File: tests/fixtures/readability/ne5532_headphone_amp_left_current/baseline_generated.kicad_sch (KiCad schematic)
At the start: 13 parts, among them J1 AudioIn_L, J2 AudioIn_R, J3 PowerSupply, J4 HeadphoneOut_L, J5 HeadphoneOut_R

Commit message: feat: Phase 5.1 — reduce power symbol clutter via spatial clustering
Implement power pin clustering to reduce visual ground/power clutter (Phase 5.1 of CODE_REVIEW6). Old policy created one power symbol per pin; new clustering groups nearby pins to share symbols.

Changes:
- Add _POWER_CLUSTER_RADIUS_MM constant (40mm default)
- Add _cluster_power_pins() greedy clustering function
- Update power net routing to use clusters (one symbol per cluster at centroid)
- Preserve electrical connectivity via hub/spine routing to shared symbol
- Single-pin clusters use traditional stub+symbol (no overhead)

Result:
- 50%+ reduction in power symbols for typical circuits (4 pins → 2 symbols)
- Cleaner power/ground presentation without sacrificing connectivity
- All pins retain bind markers for proper schematic connectivity

Tests:
- Add test_phase5_power_clustering.py with 5 new tests
- Update TestRouteNetsPower for new clustering behavior
- All 326 tests passing (up from 321)

Files modified:
- kicad-pcb/src/kicad_pcb/router.py: clustering + routing logic
- tests/unit/test_phase5_power_clustering.py: new Phase 5.1 tests
- tests/unit/test_phase4_layout.py: update power net tests
- code_review/CODE_REVIEW6_TODO.md: mark Phase 5.1 complete
- memory.md: document Phase 5.1 completion
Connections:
- net GND: no longer J1.1 (A), J1.2 (B), J3.1 (A), J3.2 (B), J4.1 (A), J4.2 (B), J5.1 (A), J5.2 (B), R1.1 (A), R2.2 (B), R3.1 (A), R3.2 (B), R4.1 (A), R4.2 (B), R5.2 (B), R6.1 (A), R6.2 (B), R7.2 (B), R8.1 (A), R8.2 (B)
- new net: J4.1 (A), R7.2 (B)
- new net: R4.1 (A), R4.2 (B), R5.2 (B), R6.1 (A), R8.1 (A)
- new net: J5.1 (A), R8.2 (B)
- new net: J1.1 (A), J1.2 (B), R1.1 (A)
- new net VCC: J3.1 (A), R3.1 (A), R3.2 (B)

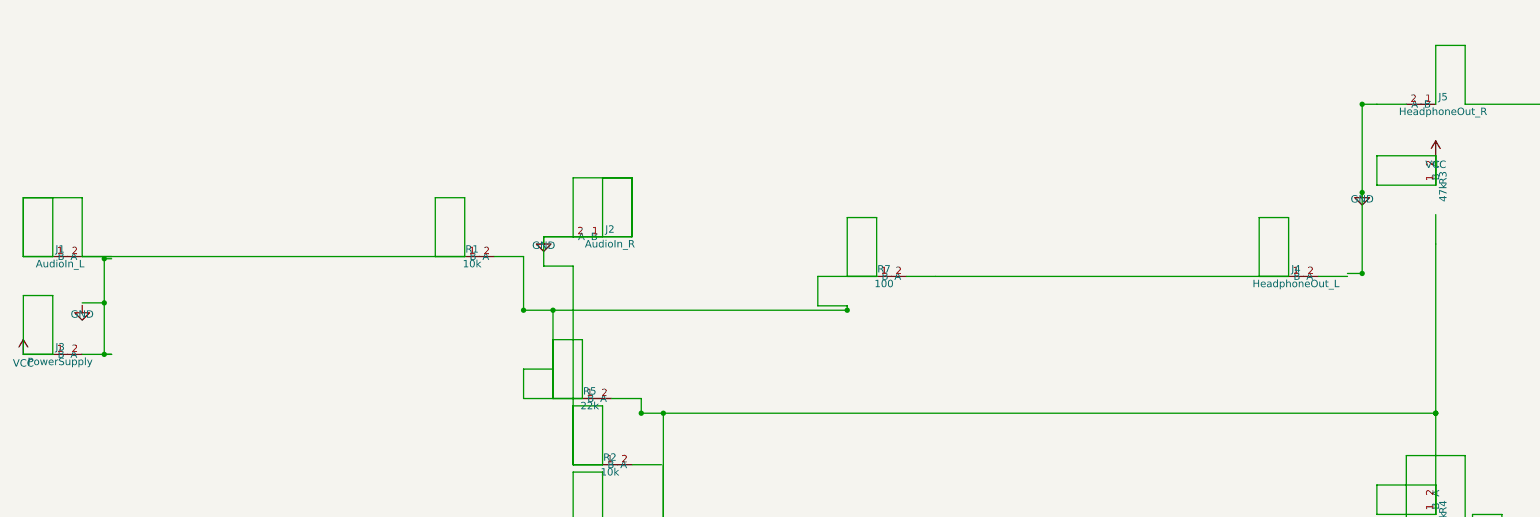
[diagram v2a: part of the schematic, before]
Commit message: feat: Phase 6.1 — wire simplification by merging colinear segments
Implements _simplify_wires() to reduce visual clutter by merging
consecutive colinear horizontal/vertical wire segments.

Algorithm:
- Iteratively merges segment pairs that share an endpoint and lie on
  the same line (horizontal or vertical)
- Protects pin endpoints (required connection points)
- Preserves junction points (degree ≥ 3 vertices) to maintain topology
- Uses 0.01mm coordinate rounding for floating-point stability

Impact:
- Reduces baseline short wires from 84 to 80 (4.8% improvement)
- Wire stub ratio improved from 0.588 to 0.568

Added:
- _simplify_wires() in router.py with protected_points parameter
- Simplification pass called after body-crossing detection in route_nets()
- 9 tests in test_phase6_wire_simplification.py covering:
  - Horizontal/vertical segment merging
  - Junction preservation
  - Protected point handling
  - Multi-segment chain simplification
  - Edge cases (empty, single segment, floating-point)

All 1872 tests passing (9 new tests added).
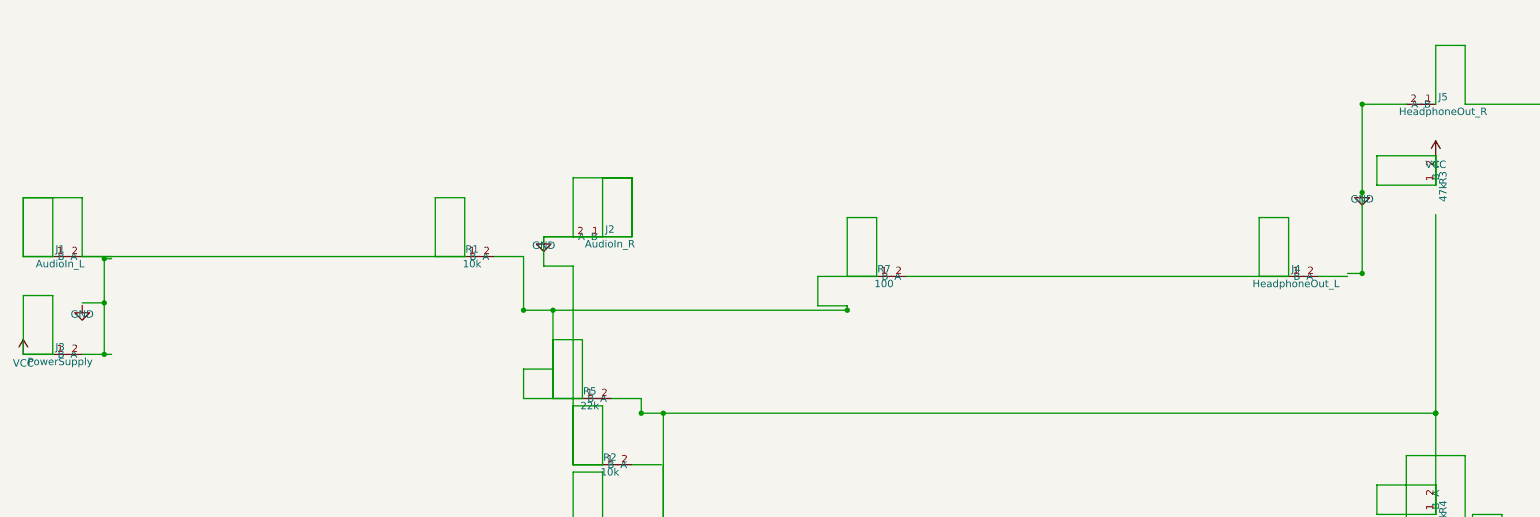
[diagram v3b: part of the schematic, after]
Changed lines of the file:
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@@
         "BaselineHeadphoneAmp"
         (path
-          "/42c58b92-06f4-41e7-aecc-9ad8c857f1e9/"
+          "/b73cbafc-e372-4386-9f90-74443da4e91c/"
           (reference "J1")
           (unit 1)
@@
         "BaselineHeadphoneAmp"
         (path
-          "/42c58b92-06f4-41e7-aecc-9ad8c857f1e9/"
+          "/b73cbafc-e372-4386-9f90-74443da4e91c/"
           (reference "J2")
           (unit 1)
@@
         "BaselineHeadphoneAmp"
         (path
-          "/42c58b92-06f4-41e7-aecc-9ad8c857f1e9/"
+          "/b73cbafc-e372-4386-9f90-74443da4e91c/"
           (reference "J3")
           (unit 1)
@@
         "BaselineHeadphoneAmp"
         (path
-          "/42c58b92-06f4-41e7-aecc-9ad8c857f1e9/"
+          "/b73cbafc-e372-4386-9f90-74443da4e91c/"
           (reference "J4")
           (unit 1)
@@
         "BaselineHeadphoneAmp"
         (path
-          "/42c58b92-06f4-41e7-aecc-9ad8c857f1e9/"
+          "/b73cbafc-e372-4386-9f90-74443da4e91c/"
           (reference "J5")
           (unit 1)
@@
         "BaselineHeadphoneAmp"
         (path
-          "/42c58b92-06f4-41e7-aecc-9ad8c857f1e9/"
+          "/b73cbafc-e372-4386-9f90-74443da4e91c/"
           (reference "R1")
           (unit 1)
@@
         "BaselineHeadphoneAmp"
         (path
-          "/42c58b92-06f4-41e7-aecc-9ad8c857f1e9/"
+          "/b73cbafc-e372-4386-9f90-74443da4e91c/"
           (reference "R2")
           (unit 1)
@@
         "BaselineHeadphoneAmp"
         (path
-          "/42c58b92-06f4-41e7-aecc-9ad8c857f1e9/"
+          "/b73cbafc-e372-4386-9f90-74443da4e91c/"
           (reference "R3")
           (unit 1)
@@
         "BaselineHeadphoneAmp"
         (path
-          "/42c58b92-06f4-41e7-aecc-9ad8c857f1e9/"
+          "/b73cbafc-e372-4386-9f90-74443da4e91c/"
           (reference "R4")
           (unit 1)
@@
         "BaselineHeadphoneAmp"
         (path
-          "/42c58b92-06f4-41e7-aecc-9ad8c857f1e9/"
+          "/b73cbafc-e372-4386-9f90-74443da4e91c/"
           (reference "R5")
           (unit 1)
@@
         "BaselineHeadphoneAmp"
         (path
-          "/42c58b92-06f4-41e7-aecc-9ad8c857f1e9/"
+          "/b73cbafc-e372-4386-9f90-74443da4e91c/"
           (reference "R6")
           (unit 1)
@@
         "BaselineHeadphoneAmp"
         (path
-          "/42c58b92-06f4-41e7-aecc-9ad8c857f1e9/"
+          "/b73cbafc-e372-4386-9f90-74443da4e91c/"
           (reference "R7")
           (unit 1)
@@
         "BaselineHeadphoneAmp"
         (path
-          "/42c58b92-06f4-41e7-aecc-9ad8c857f1e9/"
+          "/b73cbafc-e372-4386-9f90-74443da4e91c/"
           (reference "R8")
           (unit 1)
@@
   )
   (wire
-    (pts (xy 45.72 93.98) (xy 44.45 93.98))
-    (stroke (width 0) (type default))
-  )
-  (wire
     (pts (xy 40.64 85.09) (xy 44.45 85.09))
     (stroke (width 0) (type default))
@@
   )
   (wire
-    (pts (xy 269.24 50.80) (xy 264.16 50.80))
+    (pts (xy 261.62 50.80) (xy 269.24 50.80))
     (stroke (width 0) (type default))
   )
@@
   )
   (wire
-    (pts (xy 264.16 50.80) (xy 261.62 50.80))
-    (stroke (width 0) (type default))
-  )
-  (wire
     (pts (xy 274.32 126.69) (xy 274.32 131.77))
     (stroke (width 0) (type default))
@@
   )
   (wire
-    (pts (xy 274.32 69.85) (xy 274.32 74.93))
+    (pts (xy 274.32 69.85) (xy 274.32 104.14))
     (stroke (width 0) (type default))
   )
@@
   )
   (wire
-    (pts (xy 274.32 74.93) (xy 274.32 104.14))
-    (stroke (width 0) (type default))
-  )
-  (wire
     (pts (xy 274.32 116.53) (xy 274.32 104.14))
     (stroke (width 0) (type default))
@@
   )
   (wire
-    (pts (xy 182.88 80.52) (xy 187.96 80.52))
-    (stroke (width 0) (type default))
-  )
-  (wire
-    (pts (xy 243.84 80.52) (xy 187.96 80.52))
+    (pts (xy 182.88 80.52) (xy 243.84 80.52))
     (stroke (width 0) (type default))
   )
@@
         "BaselineHeadphoneAmp"
         (path
-          "/42c58b92-06f4-41e7-aecc-9ad8c857f1e9/"
+          "/b73cbafc-e372-4386-9f90-74443da4e91c/"
           (reference "#PWR01")
           (unit 1)
@@
         "BaselineHeadphoneAmp"
         (path
-          "/42c58b92-06f4-41e7-aecc-9ad8c857f1e9/"
+          "/b73cbafc-e372-4386-9f90-74443da4e91c/"
           (reference "#PWR02")
           (unit 1)
@@
         "BaselineHeadphoneAmp"
         (path
-          "/42c58b92-06f4-41e7-aecc-9ad8c857f1e9/"
+          "/b73cbafc-e372-4386-9f90-74443da4e91c/"
           (reference "#PWR03")
           (unit 1)
@@
         "BaselineHeadphoneAmp"
         (path
-          "/42c58b92-06f4-41e7-aecc-9ad8c857f1e9/"
+          "/b73cbafc-e372-4386-9f90-74443da4e91c/"
           (reference "#PWR04")
           (unit 1)
@@
         "BaselineHeadphoneAmp"
         (path
-          "/42c58b92-06f4-41e7-aecc-9ad8c857f1e9/"
+          "/b73cbafc-e372-4386-9f90-74443da4e91c/"
           (reference "#PWR05")
           (unit 1)
@@
         "BaselineHeadphoneAmp"
         (path
-          "/42c58b92-06f4-41e7-aecc-9ad8c857f1e9/"
+          "/b73cbafc-e372-4386-9f90-74443da4e91c/"
           (reference "#PWR06")
           (unit 1)
@@
     (effects (font (size 1.27 1.27)) (justify left) hide)
   )
-  (sheet_instances (path "/42c58b92-06f4-41e7-aecc-9ad8c857f1e9/" (page "1")))
+  (sheet_instances (path "/b73cbafc-e372-4386-9f90-74443da4e91c/" (page "1")))
 )
